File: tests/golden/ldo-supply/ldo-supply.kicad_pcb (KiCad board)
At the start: 2 copper layers, 40 x 36 mm, 7 parts, among them J1 CONN_PWR_1X02, J2 CONN_PWR_1X02, U1 AMS1117_3V3

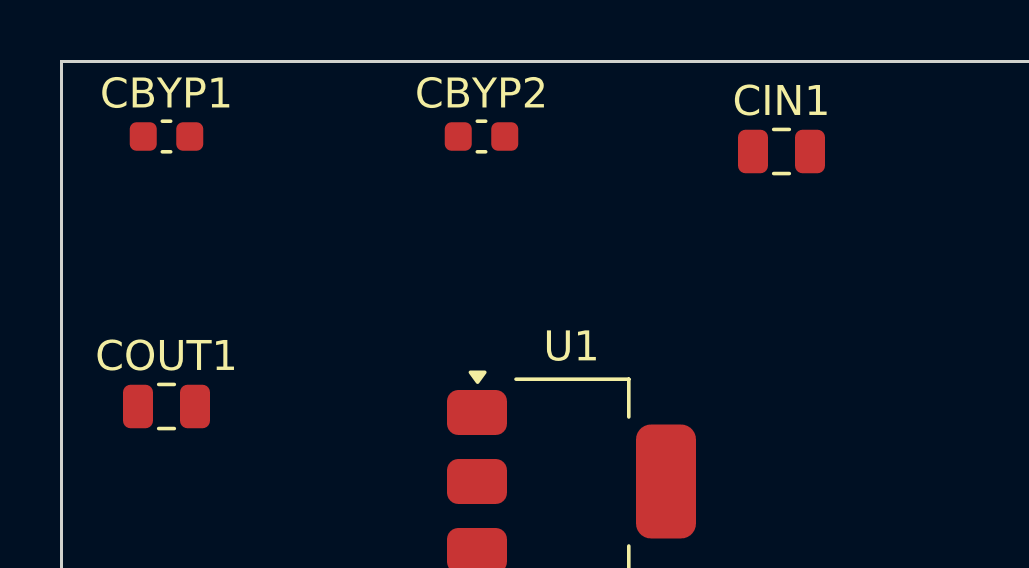
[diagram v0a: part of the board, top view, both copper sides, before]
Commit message: M5: partial reads of a design, for token economy
`aipcb summary` gives a one-line-per-block overview, and `aipcb query` narrows to
one module, component, net, net class or role. All take --json, and text and JSON
render the same structure so they cannot disagree about what a design contains.

`query module` includes the components on the *other* side of the module's ports.
A module read in isolation says nothing about what it drives, and that context is
usually the reason it is being read at all.

Also fixes automatic designator assignment. Auto-numbered parts inside a module
took their prefix from the source name, so the LDO's input capacitor became CIN1
rather than C1. Valid, but BOM tools, pick-and-place files and assembly houses all
read the prefix as the component class. Parts now carry an optional
`refdes_prefix`, which is deliberately not read from the KiCad symbol: that would
make designators depend on whether KiCad is installed, and the same source has to
produce the same board everywhere.

Co-Authored-By: Claude Opus 5 (1M context) <noreply@anthropic.com>
Claude-Session: https://claude.ai/code/session_01KUjvxrMBoskX2uCYLqdAeR
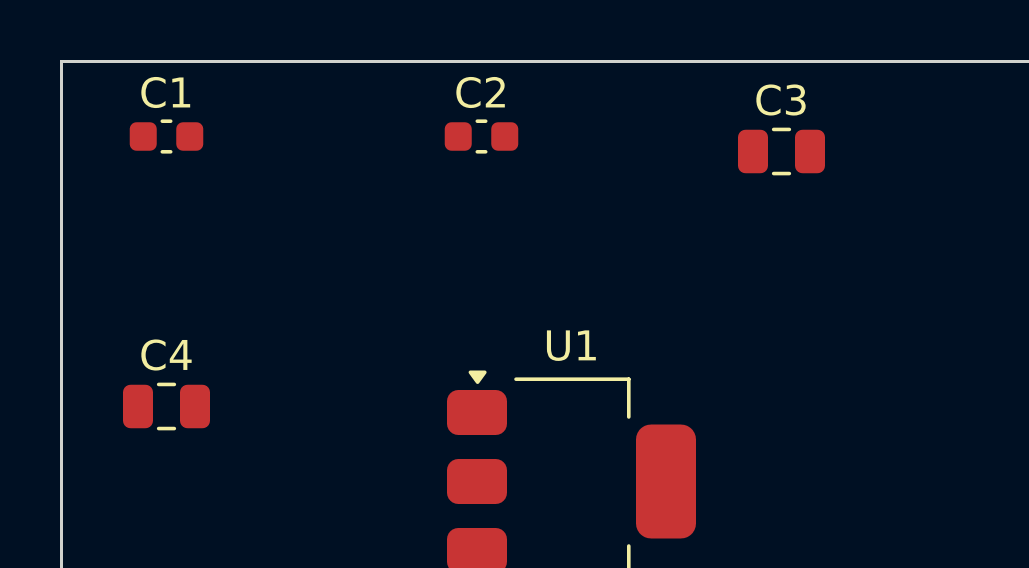
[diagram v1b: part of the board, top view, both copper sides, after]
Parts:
- renumbered CBYP1 to C1, CBYP2 to C2, CIN1 to C3, COUT1 to C4
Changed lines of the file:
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@@
 		(descr "Capacitor SMD 0603 (1608 Metric), square (rectangular) end terminal, IPC-7351 nominal, (Body size source: IPC-SM-782 page 76, https://www.pcb-3d.com/wordpress/wp-content/uploads/ipc-sm-782a_amendment_1_and_2.pdf), generated with kicad-footprint-generator")
 		(tags "capacitor")
-		(property "Reference" "CBYP1"
+		(property "Reference" "C1"
 			(at 0 -1.43 0)
 			(layer "F.SilkS")
@@
 		(descr "Capacitor SMD 0603 (1608 Metric), square (rectangular) end terminal, IPC-7351 nominal, (Body size source: IPC-SM-782 page 76, https://www.pcb-3d.com/wordpress/wp-content/uploads/ipc-sm-782a_amendment_1_and_2.pdf), generated with kicad-footprint-generator")
 		(tags "capacitor")
-		(property "Reference" "CBYP2"
+		(property "Reference" "C2"
 			(at 0 -1.43 0)
 			(layer "F.SilkS")
@@
 		(descr "Capacitor SMD 0805 (2012 Metric), square (rectangular) end terminal, IPC-7351 nominal, (Body size source: IPC-SM-782 page 76, https://www.pcb-3d.com/wordpress/wp-content/uploads/ipc-sm-782a_amendment_1_and_2.pdf, https://docs.google.com/spreadsheets/d/1BsfQQcO9C6DZCsRaXUlFlo91Tg2WpOkGARC1WS5S8t0/edit?usp=sharing), generated with kicad-footprint-generator")
 		(tags "capacitor")
-		(property "Reference" "CIN1"
+		(property "Reference" "C3"
 			(at 0 -1.68 0)
 			(layer "F.SilkS")
@@
 		(descr "Capacitor SMD 0805 (2012 Metric), square (rectangular) end terminal, IPC-7351 nominal, (Body size source: IPC-SM-782 page 76, https://www.pcb-3d.com/wordpress/wp-content/uploads/ipc-sm-782a_amendment_1_and_2.pdf, https://docs.google.com/spreadsheets/d/1BsfQQcO9C6DZCsRaXUlFlo91Tg2WpOkGARC1WS5S8t0/edit?usp=sharing), generated with kicad-footprint-generator")
 		(tags "capacitor")
-		(property "Reference" "COUT1"
+		(property "Reference" "C4"
 			(at 0 -1.68 0)
 			(layer "F.SilkS")
